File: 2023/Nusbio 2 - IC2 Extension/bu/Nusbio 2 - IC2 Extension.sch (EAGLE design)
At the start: 15 parts

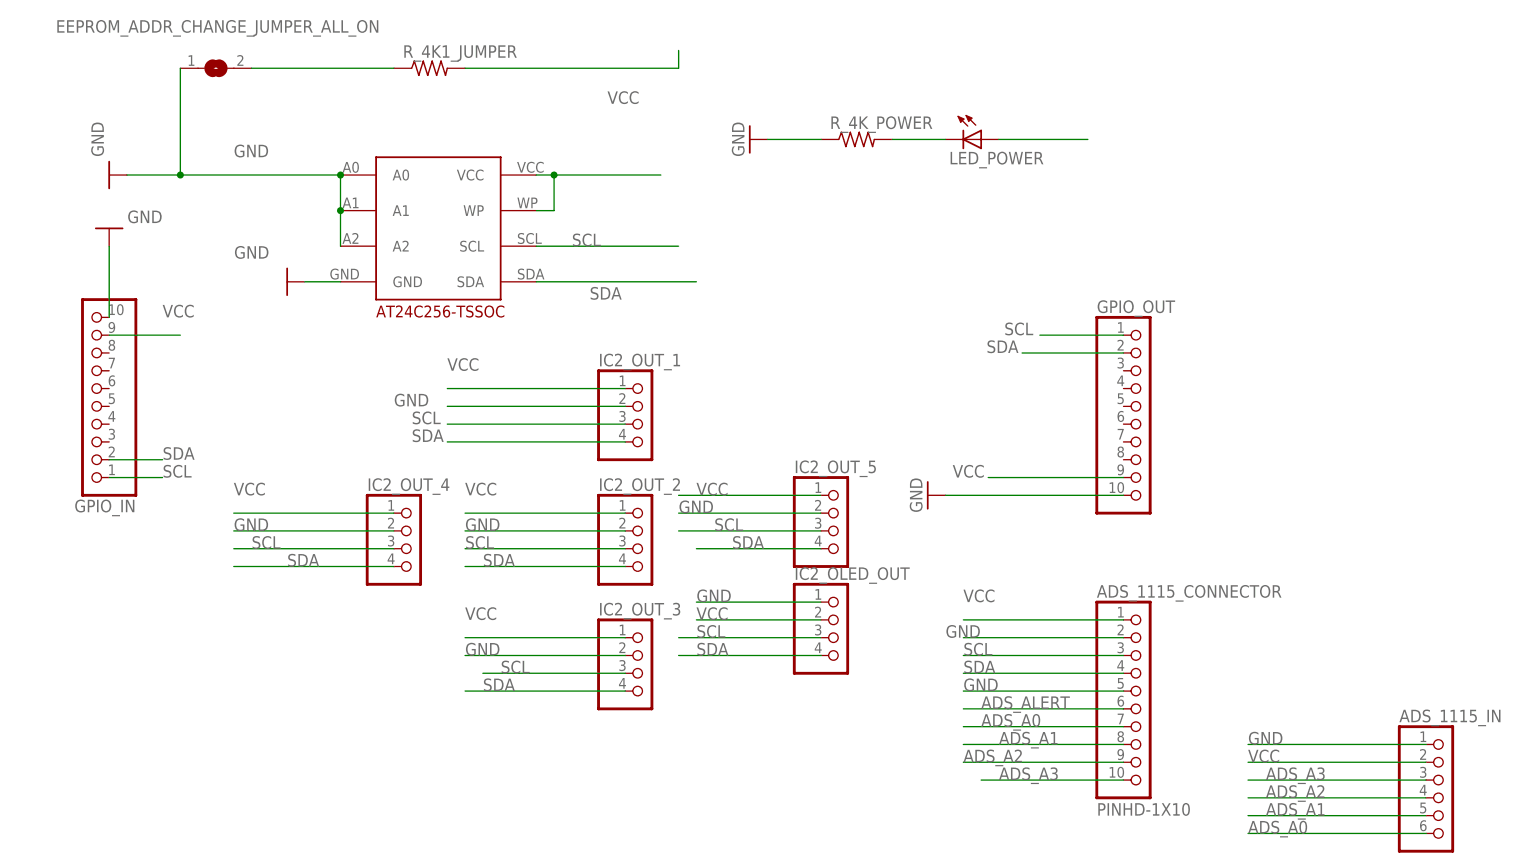
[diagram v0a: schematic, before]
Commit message: Nusbio v2 pcb and SPIExtension v 1 2023/05
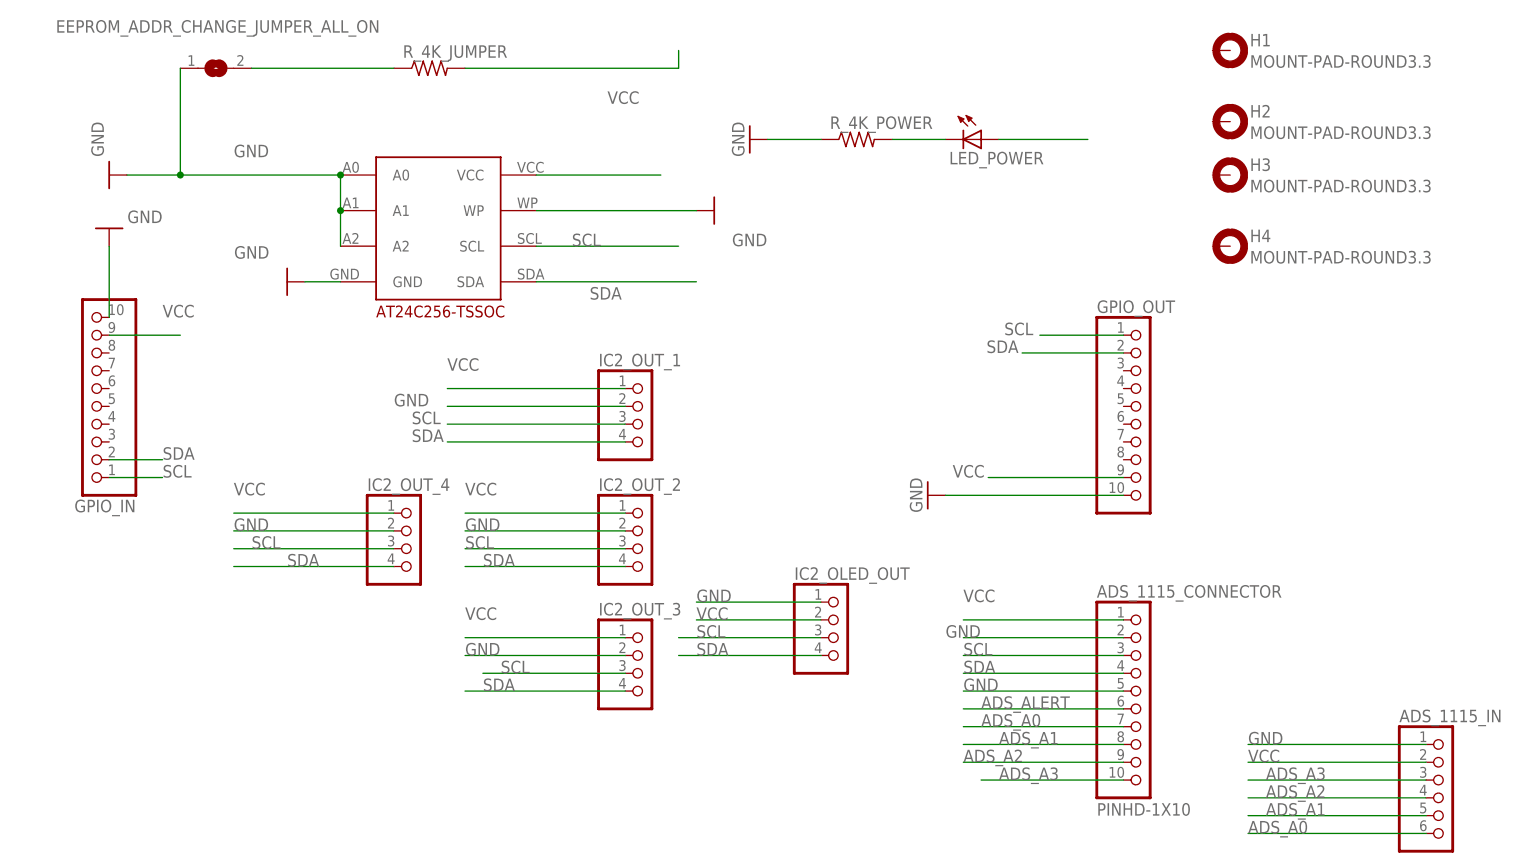
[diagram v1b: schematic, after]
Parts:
- removed IC2_OUT_5: (no value), pinhead:PINHD-1X4
- added H1, H2, H3, H4: MOUNT-PAD-ROUND3.3, holes:MOUNT-PAD-ROUND3.3
- renumbered R_4K1_JUMPER to R_4K_JUMPER
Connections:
- net GND: now also EEPROM_AT24C256.WP; no longer IC2_OUT_5.2
- net N$1: no longer EEPROM_AT24C256.WP
- net SCL: no longer IC2_OUT_5.3
- net SDA: no longer IC2_OUT_5.4
- net VCC: no longer IC2_OUT_5.1
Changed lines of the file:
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@@
 <part name="GND2" library="supply1" deviceset="GND" device=""/>
 <part name="EEPROM_ADDR_CHANGE_JUMPER_ALL_ON" library="microbuilder" deviceset="SOLDERJUMPER" device="REFLOW"/>
-<part name="R_4K1_JUMPER" library="adafruit" deviceset="R-US_" device="R1206"/>
+<part name="R_4K_JUMPER" library="adafruit" deviceset="R-US_" device="R1206"/>
 <part name="GND5" library="supply1" deviceset="GND" device=""/>
 <part name="IC2_OUT_1" library="pinhead" library_urn="urn:adsk.eagle:library:325" deviceset="PINHD-1X4" device="" package3d_urn="urn:adsk.eagle:package:22407/2"/>
@@
 <part name="IC2_OUT_3" library="pinhead" library_urn="urn:adsk.eagle:library:325" deviceset="PINHD-1X4" device="" package3d_urn="urn:adsk.eagle:package:22407/2"/>
 <part name="IC2_OUT_4" library="pinhead" library_urn="urn:adsk.eagle:library:325" deviceset="PINHD-1X4" device="" package3d_urn="urn:adsk.eagle:package:22407/2"/>
-<part name="IC2_OUT_5" library="pinhead" library_urn="urn:adsk.eagle:library:325" deviceset="PINHD-1X4" device="" package3d_urn="urn:adsk.eagle:package:22407/2"/>
 <part name="IC2_OLED_OUT" library="pinhead" library_urn="urn:adsk.eagle:library:325" deviceset="PINHD-1X4" device="" package3d_urn="urn:adsk.eagle:package:22407/2"/>
 <part name="ADS_1115_CONNECTOR" library="adafruit" deviceset="PINHD-1X10" device=""/>
 <part name="ADS_1115_IN" library="adafruit" deviceset="PINHD-1X6" device=""/>
+<part name="GND6" library="supply1" deviceset="GND" device=""/>
+<part name="H1" library="holes" library_urn="urn:adsk.eagle:library:237" deviceset="MOUNT-PAD-ROUND" device="3.3" package3d_urn="urn:adsk.eagle:package:14283/1"/>
+<part name="H2" library="holes" library_urn="urn:adsk.eagle:library:237" deviceset="MOUNT-PAD-ROUND" device="3.3" package3d_urn="urn:adsk.eagle:package:14283/1"/>
+<part name="H3" library="holes" library_urn="urn:adsk.eagle:library:237" deviceset="MOUNT-PAD-ROUND" device="3.3" package3d_urn="urn:adsk.eagle:package:14283/1"/>
+<part name="H4" library="holes" library_urn="urn:adsk.eagle:library:237" deviceset="MOUNT-PAD-ROUND" device="3.3" package3d_urn="urn:adsk.eagle:package:14283/1"/>
 </parts>
 <sheets>
@@
 <attribute name="VALUE" x="0" y="100.33" size="1.778" layer="96"/>
 </instance>
-<instance part="R_4K1_JUMPER" gate="G$1" x="33.02" y="104.14" smashed="yes">
+<instance part="R_4K_JUMPER" gate="G$1" x="33.02" y="104.14" smashed="yes">
 <attribute name="NAME" x="29.21" y="105.6386" size="1.778" layer="95"/>
 <attribute name="VALUE" x="29.21" y="100.838" size="1.778" layer="96"/>
@@
 <attribute name="VALUE" x="24.13" y="27.94" size="1.778" layer="96"/>
 </instance>
-<instance part="IC2_OUT_5" gate="A" x="91.44" y="38.1" smashed="yes">
-<attribute name="NAME" x="85.09" y="46.355" size="1.778" layer="95"/>
-<attribute name="VALUE" x="85.09" y="30.48" size="1.778" layer="96"/>
-</instance>
 <instance part="IC2_OLED_OUT" gate="A" x="91.44" y="22.86" smashed="yes">
 <attribute name="NAME" x="85.09" y="31.115" size="1.778" layer="95"/>
@@
 <attribute name="NAME" x="171.45" y="10.795" size="1.778" layer="95"/>
 <attribute name="VALUE" x="171.45" y="-10.16" size="1.778" layer="96"/>
+</instance>
+<instance part="GND6" gate="1" x="73.66" y="83.82" smashed="yes" rot="R90">
+<attribute name="VALUE" x="76.2" y="78.74" size="1.778" layer="96"/>
+</instance>
+<instance part="H1" gate="G$1" x="147.32" y="106.68" smashed="yes">
+<attribute name="NAME" x="150.114" y="107.2642" size="1.778" layer="95"/>
+<attribute name="VALUE" x="150.114" y="104.2162" size="1.778" layer="96"/>
+</instance>
+<instance part="H2" gate="G$1" x="147.32" y="96.52" smashed="yes">
+<attribute name="NAME" x="150.114" y="97.1042" size="1.778" layer="95"/>
+<attribute name="VALUE" x="150.114" y="94.0562" size="1.778" layer="96"/>
+</instance>
+<instance part="H3" gate="G$1" x="147.32" y="88.9" smashed="yes">
+<attribute name="NAME" x="150.114" y="89.4842" size="1.778" layer="95"/>
+<attribute name="VALUE" x="150.114" y="86.4362" size="1.778" layer="96"/>
+</instance>
+<instance part="H4" gate="G$1" x="147.32" y="78.74" smashed="yes">
+<attribute name="NAME" x="150.114" y="79.3242" size="1.778" layer="95"/>
+<attribute name="VALUE" x="150.114" y="76.2762" size="1.778" layer="96"/>
 </instance>
 </instances>
@@
 </segment>
 <segment>
-<pinref part="IC2_OUT_5" gate="A" pin="2"/>
-<wire x1="88.9" y1="40.64" x2="68.58" y2="40.64" width="0.1524" layer="91"/>
-<label x="68.58" y="40.64" size="1.778" layer="95"/>
-</segment>
-<segment>
 <pinref part="ADS_1115_CONNECTOR" gate="G$1" pin="2"/>
 <wire x1="132.08" y1="22.86" x2="109.22" y2="22.86" width="0.1524" layer="91"/>
@@
 <label x="71.12" y="27.94" size="1.778" layer="95"/>
 </segment>
+<segment>
+<pinref part="EEPROM_AT24C256" gate="G$1" pin="WP"/>
+<pinref part="GND6" gate="1" pin="GND"/>
+<wire x1="48.26" y1="83.82" x2="71.12" y2="83.82" width="0.1524" layer="91"/>
+</segment>
 </net>
 <net name="VCC" class="0">
@@
 </segment>
 <segment>
-<pinref part="IC2_OUT_5" gate="A" pin="1"/>
-<wire x1="88.9" y1="43.18" x2="68.58" y2="43.18" width="0.1524" layer="91"/>
-<label x="71.12" y="43.18" size="1.778" layer="95"/>
-</segment>
-<segment>
 <pinref part="ADS_1115_CONNECTOR" gate="G$1" pin="1"/>
 <wire x1="132.08" y1="25.4" x2="109.22" y2="25.4" width="0.1524" layer="91"/>
@@
 </segment>
 <segment>
-<pinref part="R_4K1_JUMPER" gate="G$1" pin="2"/>
+<pinref part="R_4K_JUMPER" gate="G$1" pin="2"/>
 <wire x1="38.1" y1="104.14" x2="68.58" y2="104.14" width="0.1524" layer="91"/>
 <wire x1="68.58" y1="104.14" x2="68.58" y2="106.68" width="0.1524" layer="91"/>
@@
 </segment>
 <segment>
-<pinref part="IC2_OUT_5" gate="A" pin="3"/>
-<wire x1="88.9" y1="38.1" x2="68.58" y2="38.1" width="0.1524" layer="91"/>
-<label x="73.66" y="38.1" size="1.778" layer="95"/>
-</segment>
-<segment>
 <pinref part="IC2_OLED_OUT" gate="A" pin="3"/>
 <wire x1="88.9" y1="22.86" x2="68.58" y2="22.86" width="0.1524" layer="91"/>
@@
 </segment>
 <segment>
-<pinref part="IC2_OUT_5" gate="A" pin="4"/>
-<wire x1="88.9" y1="35.56" x2="71.12" y2="35.56" width="0.1524" layer="91"/>
-<label x="76.2" y="35.56" size="1.778" layer="95"/>
-</segment>
-<segment>
 <pinref part="IC2_OLED_OUT" gate="A" pin="4"/>
 <wire x1="88.9" y1="20.32" x2="68.58" y2="20.32" width="0.1524" layer="91"/>
@@
 <segment>
 <pinref part="EEPROM_AT24C256" gate="G$1" pin="VCC"/>
-<wire x1="48.26" y1="88.9" x2="50.8" y2="88.9" width="0.1524" layer="91"/>
-<pinref part="EEPROM_AT24C256" gate="G$1" pin="WP"/>
-<wire x1="50.8" y1="88.9" x2="66.04" y2="88.9" width="0.1524" layer="91"/>
-<wire x1="48.26" y1="83.82" x2="50.8" y2="83.82" width="0.1524" layer="91"/>
-<wire x1="50.8" y1="83.82" x2="50.8" y2="88.9" width="0.1524" layer="91"/>
-<junction x="50.8" y="88.9"/>
+<wire x1="48.26" y1="88.9" x2="66.04" y2="88.9" width="0.1524" layer="91"/>
 </segment>
 </net>
 <net name="N$6" class="0">
 <segment>
-<pinref part="R_4K1_JUMPER" gate="G$1" pin="1"/>
+<pinref part="R_4K_JUMPER" gate="G$1" pin="1"/>
 <pinref part="EEPROM_ADDR_CHANGE_JUMPER_ALL_ON" gate="1" pin="2"/>
 <wire x1="27.94" y1="104.14" x2="7.62" y2="104.14" width="0.1524" layer="91"/>
